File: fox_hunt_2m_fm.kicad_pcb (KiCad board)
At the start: 2 copper layers, 50.9 x 55.1 mm, 19 parts, among them J1 I/O 1, J2 I/O 2, J3 BATT, J4 Ext Wire Ant, Q1 BSS138K, U1 MAX2606, U2 SMA3107

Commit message: Rev B
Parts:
- removed R1, R2: 1k, Resistor_SMD:R_1206_3216Metric_Pad1.30x1.75mm_HandSolder
- added D1: D, Diode_THT:D_DO-35_SOD27_P7.62mm_Horizontal, F.Cu at (147.2, 136.0)
- added L2: 330nH, Inductor_SMD:L_1008_2520Metric, F.Cu at (155.2, 115.7)
- added L3: 330nH, Inductor_SMD:L_1008_2520Metric, F.Cu at (162.5, 121.4)
- BT1: moved to F.Cu
- moved L1 2.74 mm to (155.6, 122.5)
- moved C5 1.63 mm to (162.2, 126.1)
- moved C3 0.28 mm to (158.6, 129.9)
- turned BT1 to 270 degrees
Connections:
- C3 pad 2: +3V3 -> Net-(C3-Pad2)
- J3 pad 2: Net-(BT1-Pad1) -> Net-(D1-Pad1)
- U1 pad 6: Net-(R1-Pad2) -> Net-(C3-Pad2)
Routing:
- net Net-(BT1-Pad1): track 41.8 -> 5.28 mm
- net Net-(D1-Pad1): track 0.00 -> 31.8 mm
- net Net-(C3-Pad2): track 0.00 -> 17.8 mm
- net +3V3: track 63.2 -> 54.7 mm
- net Net-(R1-Pad2): track 8.02 -> 0.00 mm
- net Net-(L3-Pad2): track 11.3 -> 7.26 mm
- net GND: track 19.2 -> 23.0 mm, vias 151 -> 156
- net Net-(L1-Pad2): track 5.23 -> 2.53 mm
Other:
- net class Signal added: clearance 0.2, trace_width 10, via_dia 0.8, via_drill 0.4
- net class VCC added: clearance 0.2, trace_width 0.4, via_dia 0.8, via_drill 0.4
- board text added: "2m Fox rev. B"

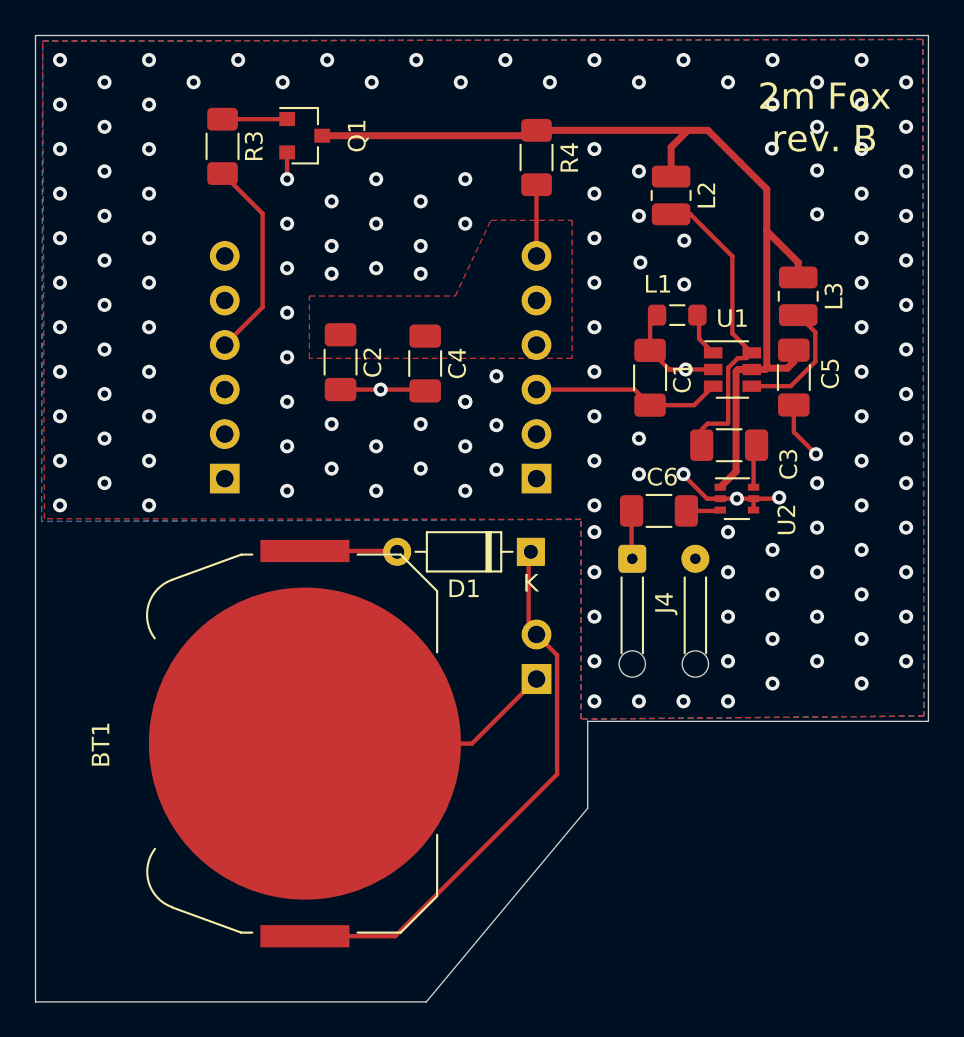
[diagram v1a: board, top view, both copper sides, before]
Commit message: Board and schematic Rev. C
Use IO line to directly power analog section.
Remove power MOSFET as it's not needed.
Add additional filter cap.
Rearrange PCB to account for above.
Add antenna length to silkscreen.
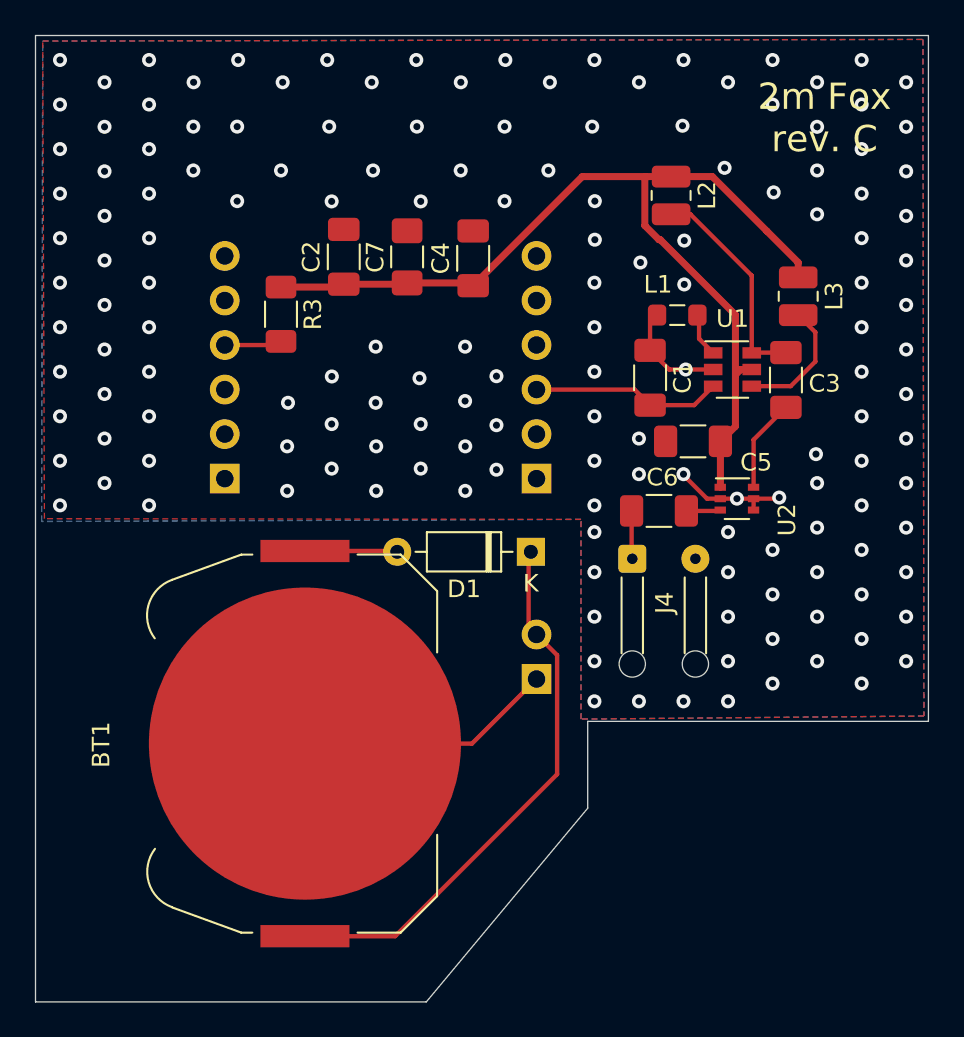
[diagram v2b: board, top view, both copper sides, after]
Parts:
- removed Q1: BSS138K, Package_TO_SOT_SMD:SOT-23
- removed R4: 15, Resistor_SMD:R_1206_3216Metric_Pad1.30x1.75mm_HandSolder
- added C7: 470pF, Capacitor_SMD:C_1206_3216Metric_Pad1.42x1.75mm_HandSolder, F.Cu at (140.2, 119.2)
- moved R3 10.1 mm to (133.0, 122.5)
- moved C5 6.80 mm to (156.5, 129.7), turned to 0 degrees
- moved C4 6.59 mm to (144.0, 119.3), turned to 90 degrees
- moved C2 6.01 mm to (136.6, 119.2), turned to 90 degrees
- moved C3 4.93 mm to (161.8, 126.2), turned to 90 degrees
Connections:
- C2 pad 1: VCC -> +3V3
- C4 pad 1: VCC -> +3V3
- J1 pad 4: VCC -> Net-(J1-Pad4)
- J1 pad 5: VCC -> Net-(J1-Pad5)
- J1 pad 6: VCC -> Net-(J1-Pad6)
- R3 pad 1: Net-(Q1-Pad1) -> +3V3
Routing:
- net GND: track 23.0 -> 13.3 mm, vias 156 -> 157
- net Net-(J2-Pad4): track 11.6 -> 3.29 mm
- net Net-(C3-Pad2): track 17.8 -> 12.4 mm
- net VCC: track 4.06 -> 0.00 mm
- net Net-(Q1-Pad1): track 3.69 -> 0.00 mm
- net Net-(C3-Pad1): track 2.58 -> 5.32 mm
- net +3V3: track 54.7 -> 56.5 mm
- removed copper zone on F.Cu, net VCC
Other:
- board text added: "2m Fox rev. C"
- board text added: "Each 20.5”"
- board text removed: "2m Fox rev. B"
